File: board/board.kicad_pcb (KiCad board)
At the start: 2 copper layers, 50.8 x 33 mm, 80 parts, among them IC1 LVC245A, IC2 LVC245A, J1 Conn_01x11_Male, J10 Conn_01x01_Male, J2 AudioJack4_Ground, J3 Conn_01x01_Male, J4 Conn_01x01_Male, J5 Conn_01x01_Male, J6 Conn_01x01_Male, J7 Conn_01x01_Male, J8 Conn_01x01_Male, J9 Conn_01x01_Male, U1 THS7316, U2 10M02SCE144

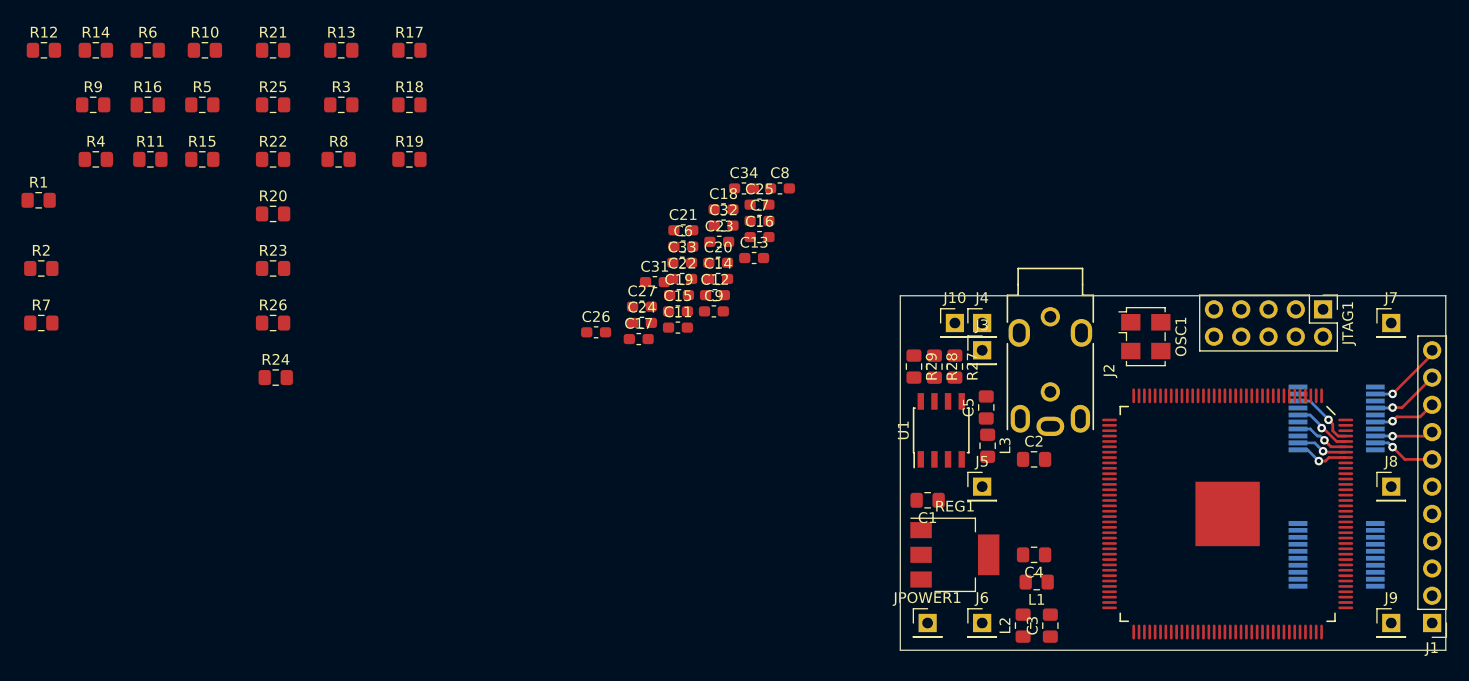
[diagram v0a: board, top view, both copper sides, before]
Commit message: Ongoing design
Squeezing all necessary electronics onto a 3.3mm x 5.1mm board
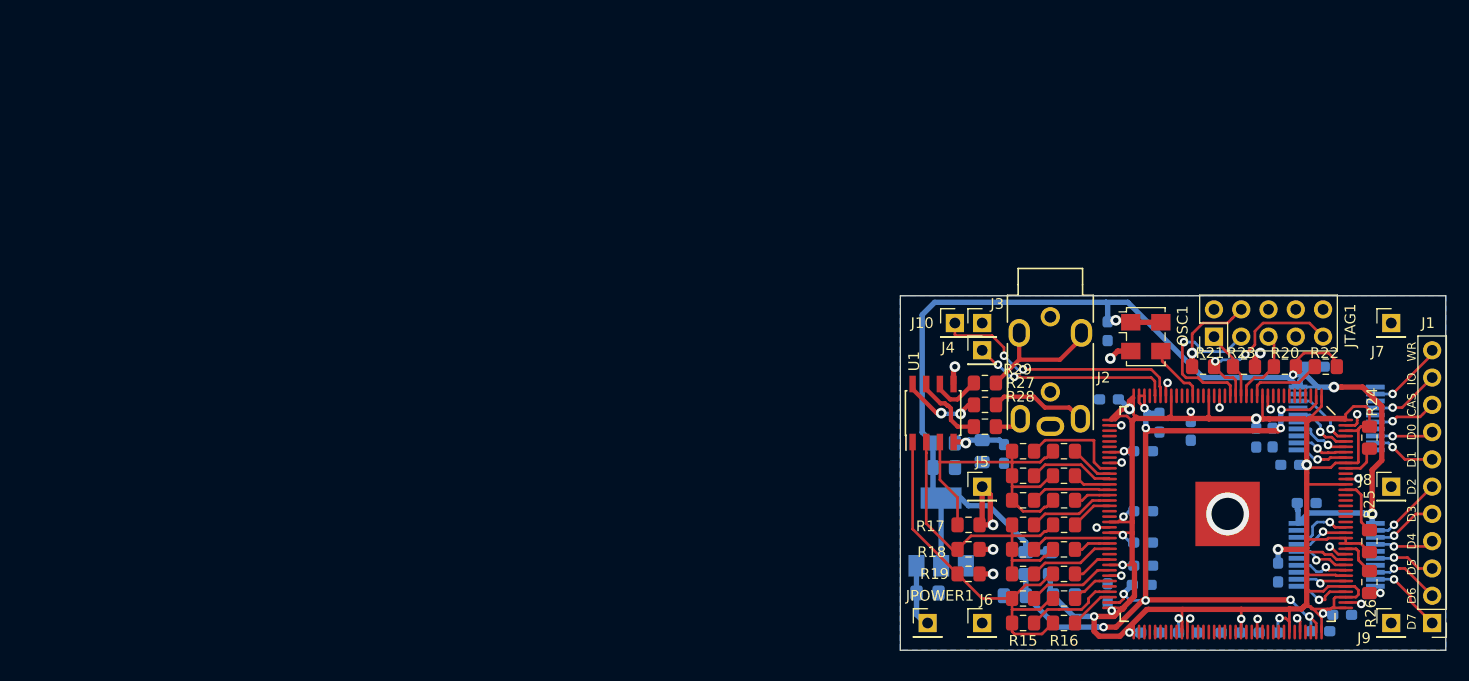
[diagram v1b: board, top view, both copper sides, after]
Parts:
- removed C26, C27: 100nF, Capacitor_SMD:C_0603_1608Metric_Pad1.05x0.95mm_HandSolder
- C1, C11, C12, C13, C14, C15, C16, C17, C18, C19, C2, C20, C21, C22, C23, C24, C25, C3, C31, C32, C33, C34, C4, C5, C6, C7, C8, C9, L1, L2, L3, REG1: moved to B.Cu
- moved R25 109.9 mm to (221.5, 116.8), turned to 90 degrees
- moved R12 106.8 mm to (193.0, 119.9), turned to 180 degrees
- moved R26 104.9 mm to (221.5, 120.7), turned to 90 degrees
- moved R14 103.6 mm to (193.0, 122.2), turned to 180 degrees
- moved R24 102.0 mm to (221.5, 107.2), turned to 270 degrees
- moved R22 99.9 mm to (217.4, 100.6)
- moved R16 98.0 mm to (193.0, 124.5), turned to 180 degrees
- moved R2 96.8 mm to (193.0, 108.5), turned to 180 degrees
- moved R9 96.0 mm to (189.2, 117.6), turned to 180 degrees
- moved R20 95.3 mm to (213.6, 100.6)
- moved R6 95.1 mm to (193.0, 113.0), turned to 180 degrees
- moved R4 94.9 mm to (193.0, 110.7), turned to 180 degrees
- moved R1 94.6 mm to (189.2, 108.5), turned to 180 degrees
- moved R7 93.4 mm to (189.2, 115.3), turned to 180 degrees
- moved R10 92.5 mm to (193.0, 117.6), turned to 180 degrees
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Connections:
- net Net-(R28-Pad2) renamed /PB2
- J10 pad 1: /SCANLINES -> /LINEDOUBLE
- J3 pad 1: /LINEDOUBLE -> /SCANLINES
- R27 pad 2: Net-(R27-Pad2) -> /PR2
- R29 pad 2: Net-(R29-Pad2) -> /Y2
- U1 pad 1: Net-(R1-Pad2) -> Net-(R12-Pad2)
- U1 pad 3: Net-(R12-Pad2) -> Net-(R1-Pad2)
- U1 pad 6: Net-(R27-Pad2) -> /Y2
- U1 pad 8: Net-(R29-Pad2) -> /PR2
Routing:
- net /3V3B: track 0.00 -> 205.9 mm, vias 0 -> 16
- net /3V3A: track 0.00 -> 138.6 mm, vias 0 -> 5
- net /3V3C: track 0.00 -> 82.0 mm, vias 0 -> 9
- net GND: track 0.00 -> 36.6 mm, vias 0 -> 22
- net Net-(R12-Pad2): track 0.00 -> 36.5 mm
- net Net-(R1-Pad2): track 0.00 -> 32.8 mm
- net Net-(R10-Pad2): track 0.00 -> 30.2 mm
- net /LINEDOUBLE: track 0.00 -> 24.0 mm, vias 0 -> 2
- net /SCANLINES: track 0.00 -> 18.7 mm, vias 0 -> 2
- net Net-(JTAG1-Pad9): track 0.00 -> 17.3 mm, vias 0 -> 2
- net Net-(JTAG1-Pad3): track 0.00 -> 15.2 mm, vias 0 -> 1
- net /Y: track 0.00 -> 12.7 mm
- net Net-(R1-Pad1): track 0.00 -> 9.72 mm
- net /PR: track 0.00 -> 9.03 mm
- net Net-(R15-Pad1): track 0.00 -> 8.46 mm
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- added copper zone on B.Cu, net GND
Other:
- net class power added: clearance 0.2, trace_width 0.5, via_dia 1, via_drill 0.7
- net class video added: clearance 0.2, trace_width 0.4, via_dia 1, via_drill 0.6
- board text added: "CAS"
- board text added: "D0"
- board text added: "D1"
- board text added: "D2"
- board text added: "D3"
- board text added: "D4"
- board text added: "D5"
- board text added: "D6"
- board text added: "D7"
- board text added: "IO"
- board text added: "WR"
- board text added: "github.com/c0pperdragon/ ZX-Spectrum-Component-Video"

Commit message: Layout complete (version 1)
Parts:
- added J11: Conn_01x05_Male, Connector_PinHeader_2.54mm:PinHeader_1x05_P2.54mm_Vertical, F.Cu at (227.3, 124.5)
- J1: value Conn_01x11_Male -> Conn_01x06_Male; footprint Connector_PinHeader_2.54mm:PinHeader_1x11_P2.54mm_Vertical -> Connector_PinHeader_2.54mm:PinHeader_1x06_P2.54mm_Vertical
- moved J1 15.2 mm to (227.3, 109.2)
- moved J8 2.09 mm to (225.6, 112.3)
- moved J5 1.14 mm to (186.4, 112.3)
- moved R3 0.51 mm to (189.7, 110.7)
- moved R4 0.51 mm to (193.5, 110.7)
- moved R5 0.51 mm to (189.7, 113.0)
- moved R8 0.50 mm to (193.5, 115.3)
- moved R6 0.49 mm to (193.5, 113.0)
- moved R10 0.13 mm to (193.2, 117.6)
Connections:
- J1 pad 1: /D7 -> /D2
- J1 pad 2: /D6 -> /D1
- J1 pad 3: /D5 -> /D0
- J1 pad 4: /D4 -> /CAS
- J1 pad 5: /D3 -> /IOREQ
- J1 pad 6: /D2 -> /WR
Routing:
- net /D2: track 6.98 -> 10.9 mm
- net /WR: track 7.20 -> 9.74 mm
- net /IOREQ: track 6.46 -> 8.48 mm
- net Net-(R10-Pad2): track 30.2 -> 31.9 mm
- net Net-(R1-Pad1): track 9.72 -> 11.3 mm, vias 0 -> 2
- net /CAS: track 5.95 -> 7.23 mm
- net Net-(R12-Pad2): track 36.5 -> 37.7 mm
- net /D0: track 5.46 -> 6.51 mm
- net Net-(R1-Pad2): track 32.8 -> 33.7 mm
- net Net-(R4-Pad1): track 3.55 -> 3.04 mm

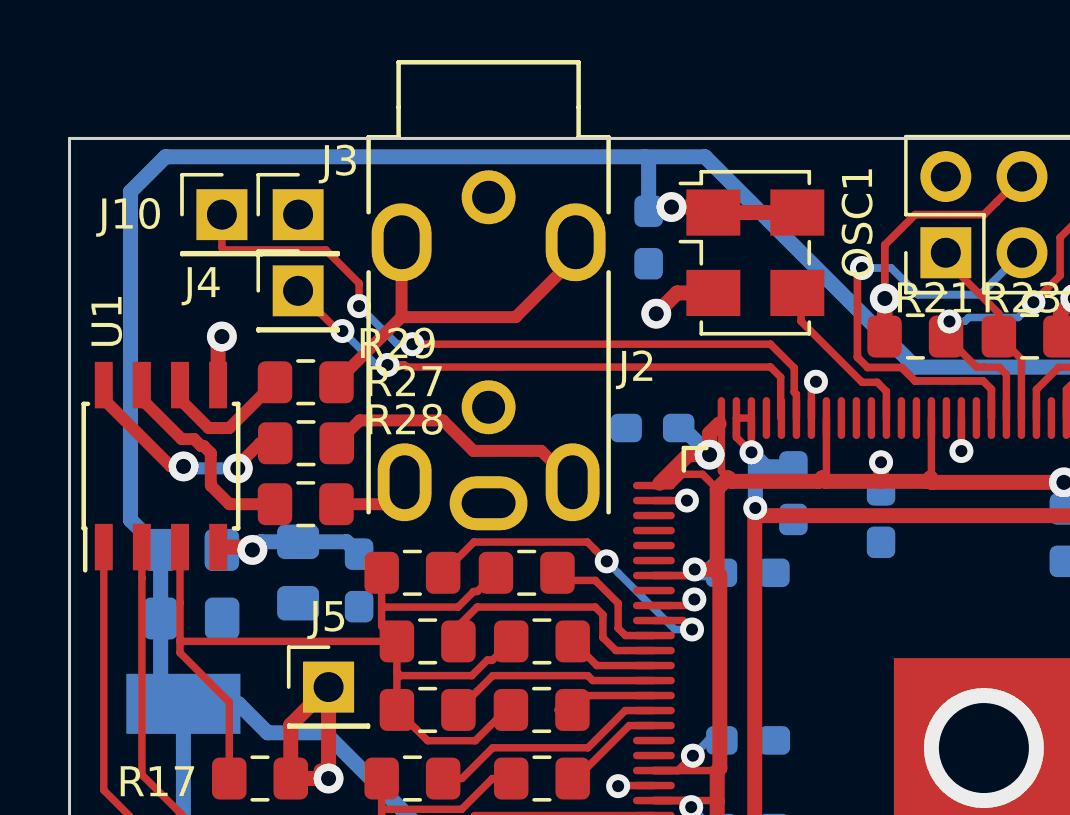
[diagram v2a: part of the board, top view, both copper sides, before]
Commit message: Redesign mode jumpers. Minor fixes in silk screen.
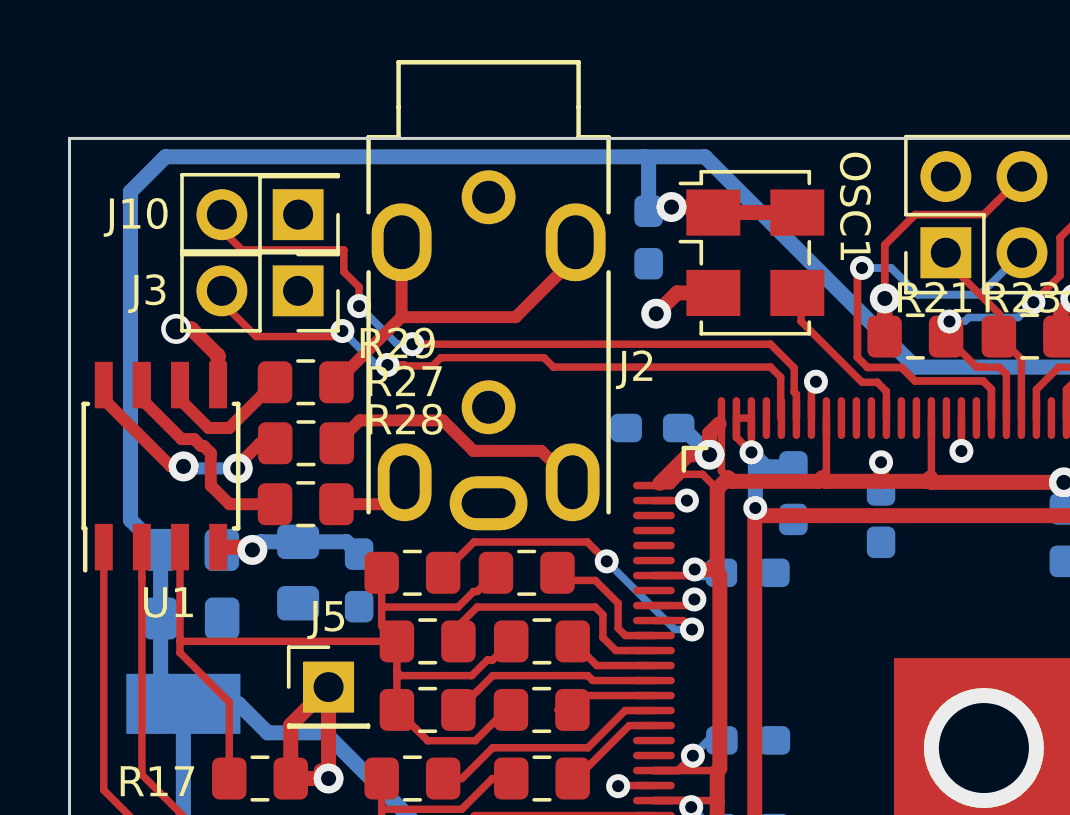
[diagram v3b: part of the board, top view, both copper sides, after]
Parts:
- removed J4: Conn_01x01_Male, Connector_PinHeader_2.54mm:PinHeader_1x01_P2.54mm_Vertical
- J10, J3: value Conn_01x01_Male -> Conn_01x02; footprint Connector_PinHeader_2.54mm:PinHeader_1x01_P2.54mm_Vertical -> Connector_PinHeader_2.54mm:PinHeader_2x01_P2.54mm_Vertical
- moved J10 2.54 mm to (185.4, 96.5), turned to 180 degrees
- turned J3 to 180 degrees
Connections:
- J10 pad 1: /LINEDOUBLE -> GND
- J3 pad 1: /SCANLINES -> GND
- U2 pad 32: /SCANLINES -> /RGBMODE
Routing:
- net /RGBMODE: track 0.00 -> 21.9 mm, vias 0 -> 2
- net /SCANLINES: track 18.7 -> 0.00 mm, vias 2 -> 0
- net GND: track 36.2 -> 37.3 mm

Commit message: Modify PCB for easier assembly
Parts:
- moved C9 5.09 mm to (220.7, 112.9)
- moved C8 4.71 mm to (221.1, 100.3)
- moved C7 4.70 mm to (185.9, 104.3), turned to 270 degrees
- moved C24 2.08 mm to (220.2, 125.3)
- moved C12 2.01 mm to (209.0, 106.6)
- moved C25 1.95 mm to (211.3, 118.7)
- moved C11 1.52 mm to (212.7, 110.4)
- moved L2 1.49 mm to (189.0, 117.5)
- moved L1 1.41 mm to (191.8, 117.5)
- moved C1 0.89 mm to (180.3, 122.6)
- moved C32 0.88 mm to (201.9, 104.9)
- moved C16 0.77 mm to (200.5, 116.2)
- moved C31 0.73 mm to (212.0, 107.7)
- moved C5 0.64 mm to (186.1, 108.4)
- moved C33 0.52 mm to (216.4, 125.3)
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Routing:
- net /3V3C: track 82.0 -> 86.1 mm
- net /D7: track 7.28 -> 11.0 mm
- net /3V3B: track 206.2 -> 209.6 mm
- net /D1: track 6.03 -> 9.11 mm
- net /3V3A: track 138.6 -> 137.3 mm
- net /3V3D: track 6.04 -> 6.96 mm
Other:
- board text added: "1"
- board text added: "ZX-Spectrum Component Video Rev. 2"
- board text added: "github.com/c0pperdragon"
- board text removed: "github.com/c0pperdragon/ ZX-Spectrum-Component-Video"
